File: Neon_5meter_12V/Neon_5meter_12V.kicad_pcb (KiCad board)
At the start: 2 copper layers, 77.5 x 51.5 mm, 47 parts, among them J2 Barrel_Jack_MountingPin, J4 Barrel_Jack_MountingPin, J5 Barrel_Jack_MountingPin, J6 Conn_01x03_Pin, Q1 IRLML2502TRPBF, Q2 IRLML2502TRPBF, Q3 BSS138, Q4 BSS138, Q5 BSS138, SW1 SW_Push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

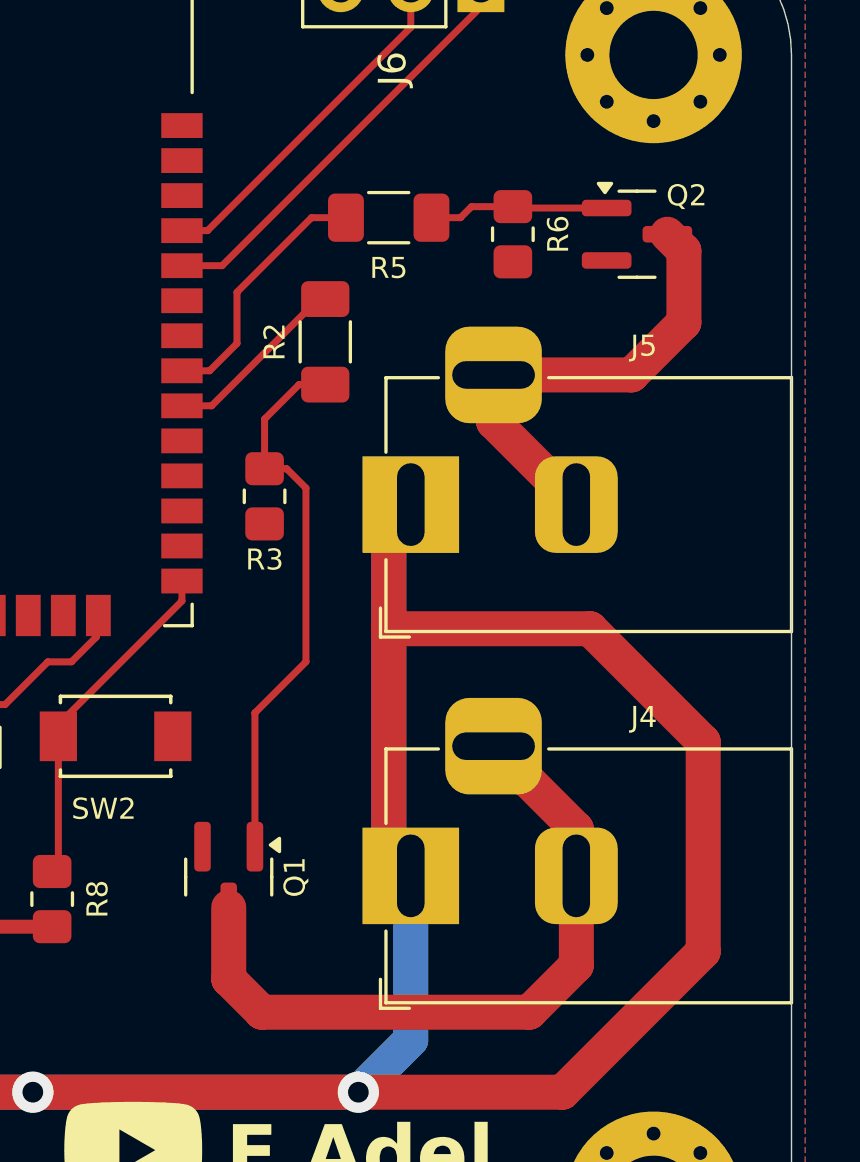
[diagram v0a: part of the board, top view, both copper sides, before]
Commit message: added custom sot23 foorprint and 3d model
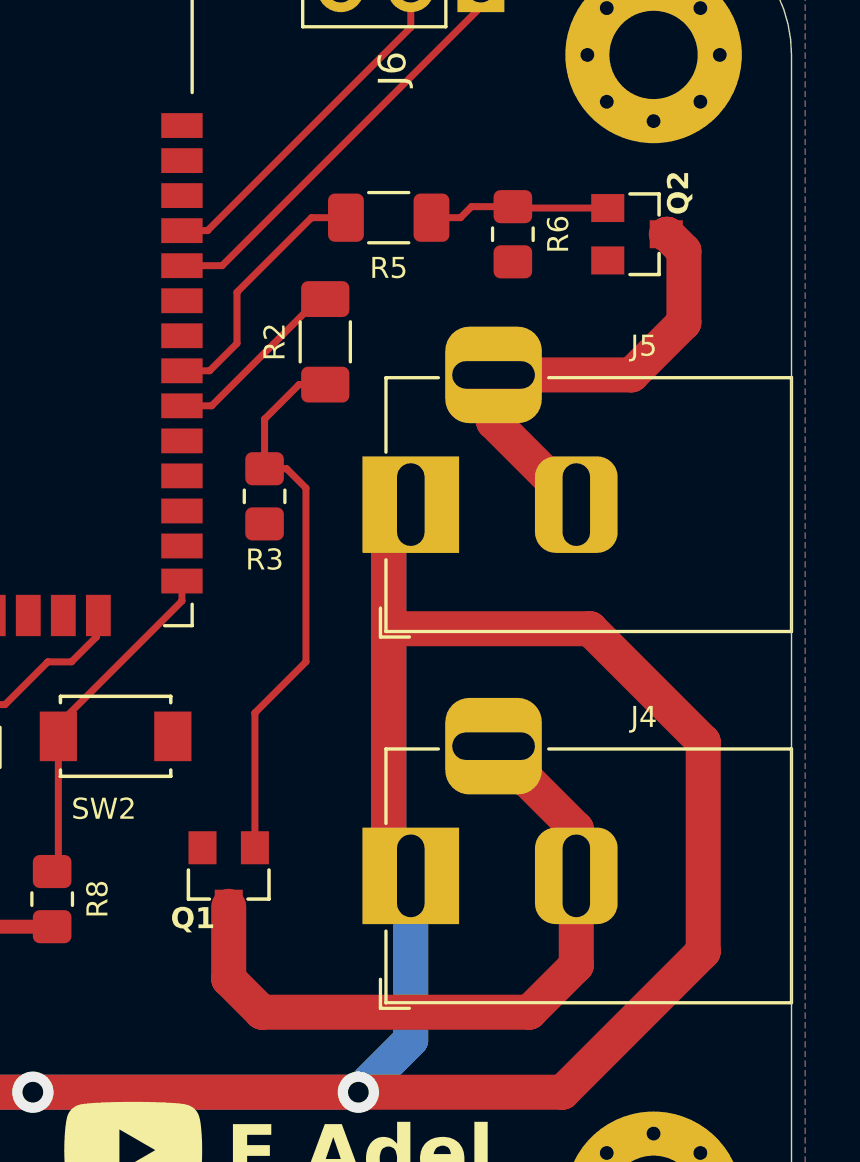
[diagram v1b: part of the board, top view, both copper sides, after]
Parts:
- Q1, Q2: footprint Package_TO_SOT_SMD:SOT-23 -> custom_SOT23:custom_SOT23
- turned Q1 to 180 degrees
- turned Q2 to -90 degrees
